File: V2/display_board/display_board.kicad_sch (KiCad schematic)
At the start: 52 parts, among them J1 Conn_01x12, J2 Conn_01x12, Q1 Si1308EDL, SW1 SW_Push, SW2 SW_Push, SW3 SW_Push, SW4 SW_Push, U1 TPS61165DBV, U2 LTR-303ALS-01, U3 DS18B20Z

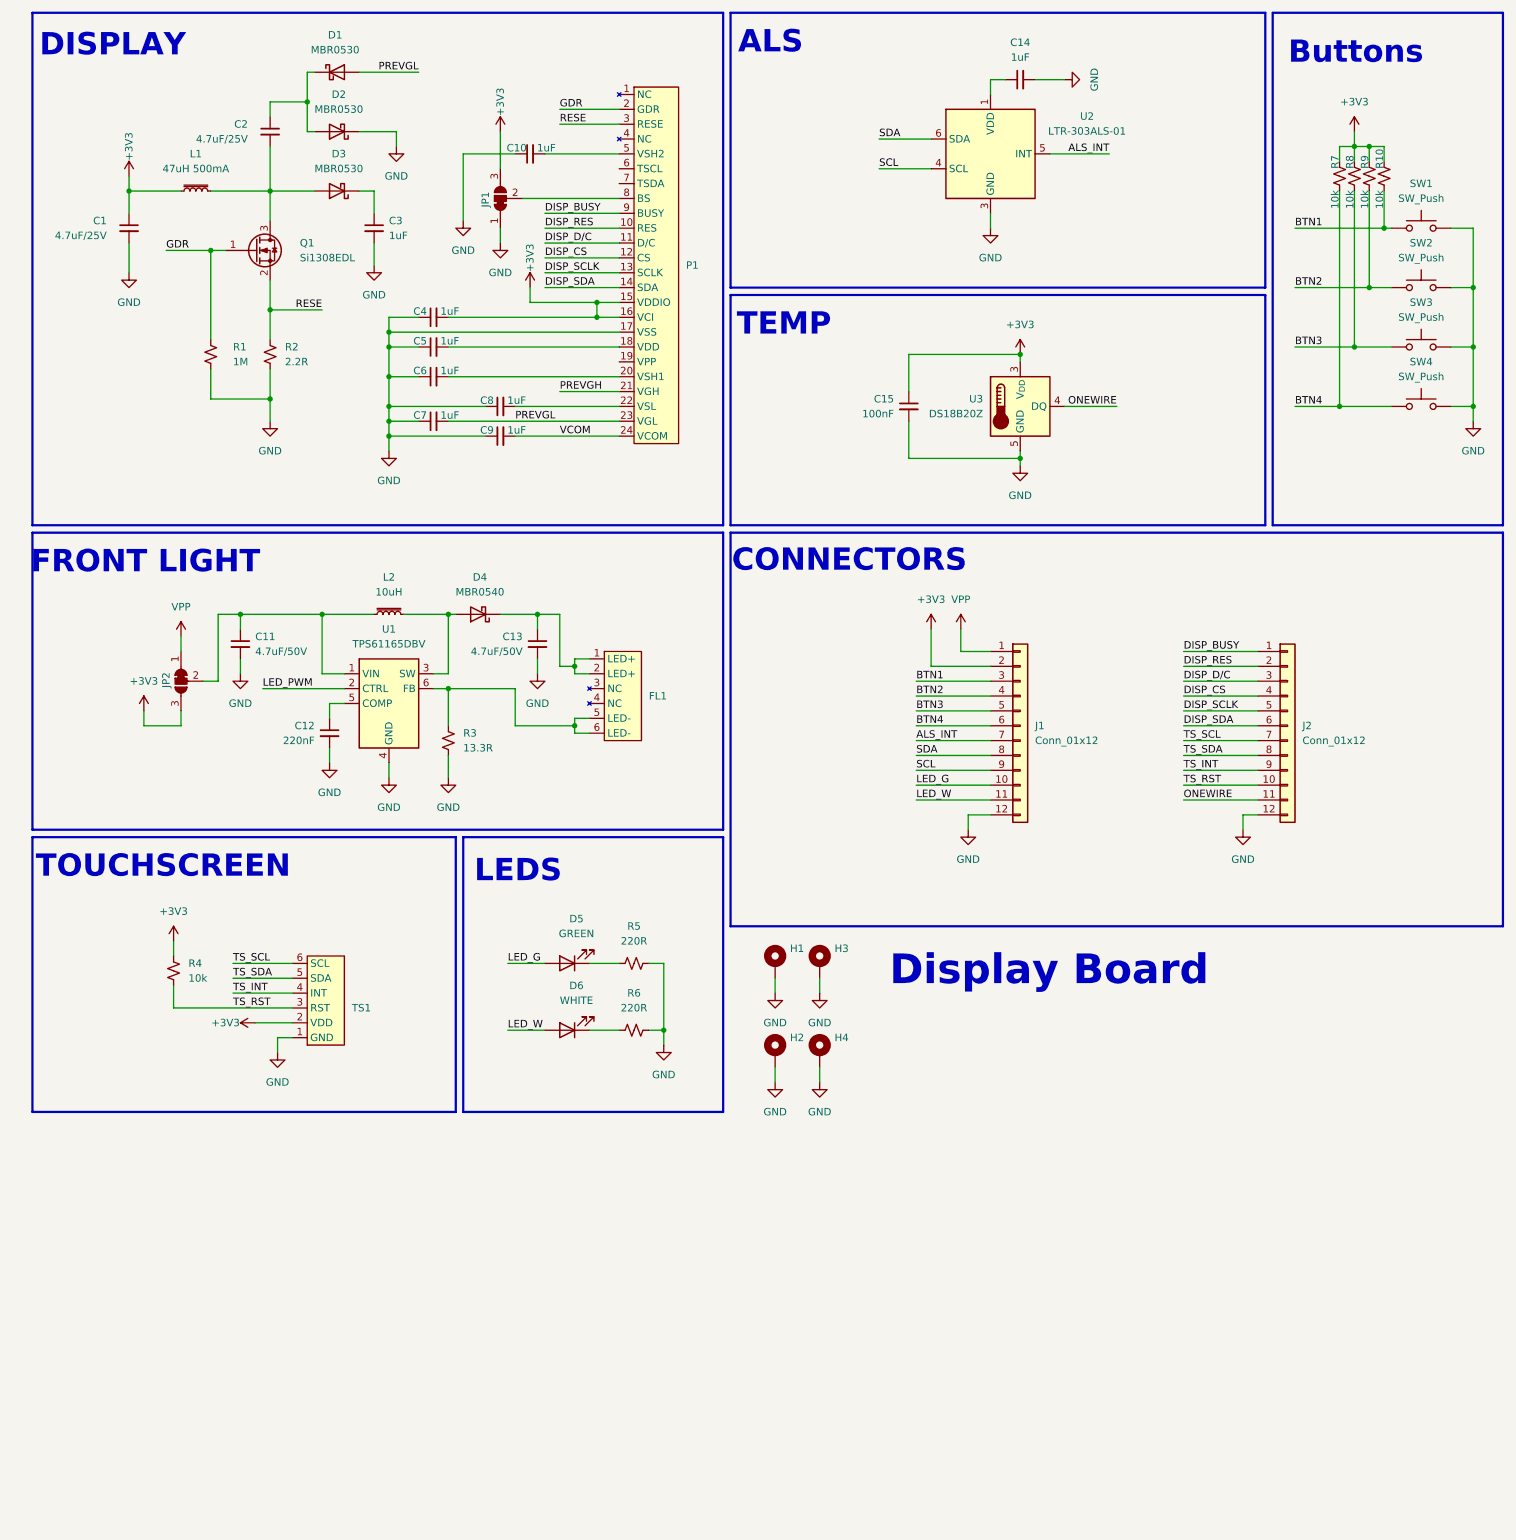
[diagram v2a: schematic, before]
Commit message: Initial component placement done.
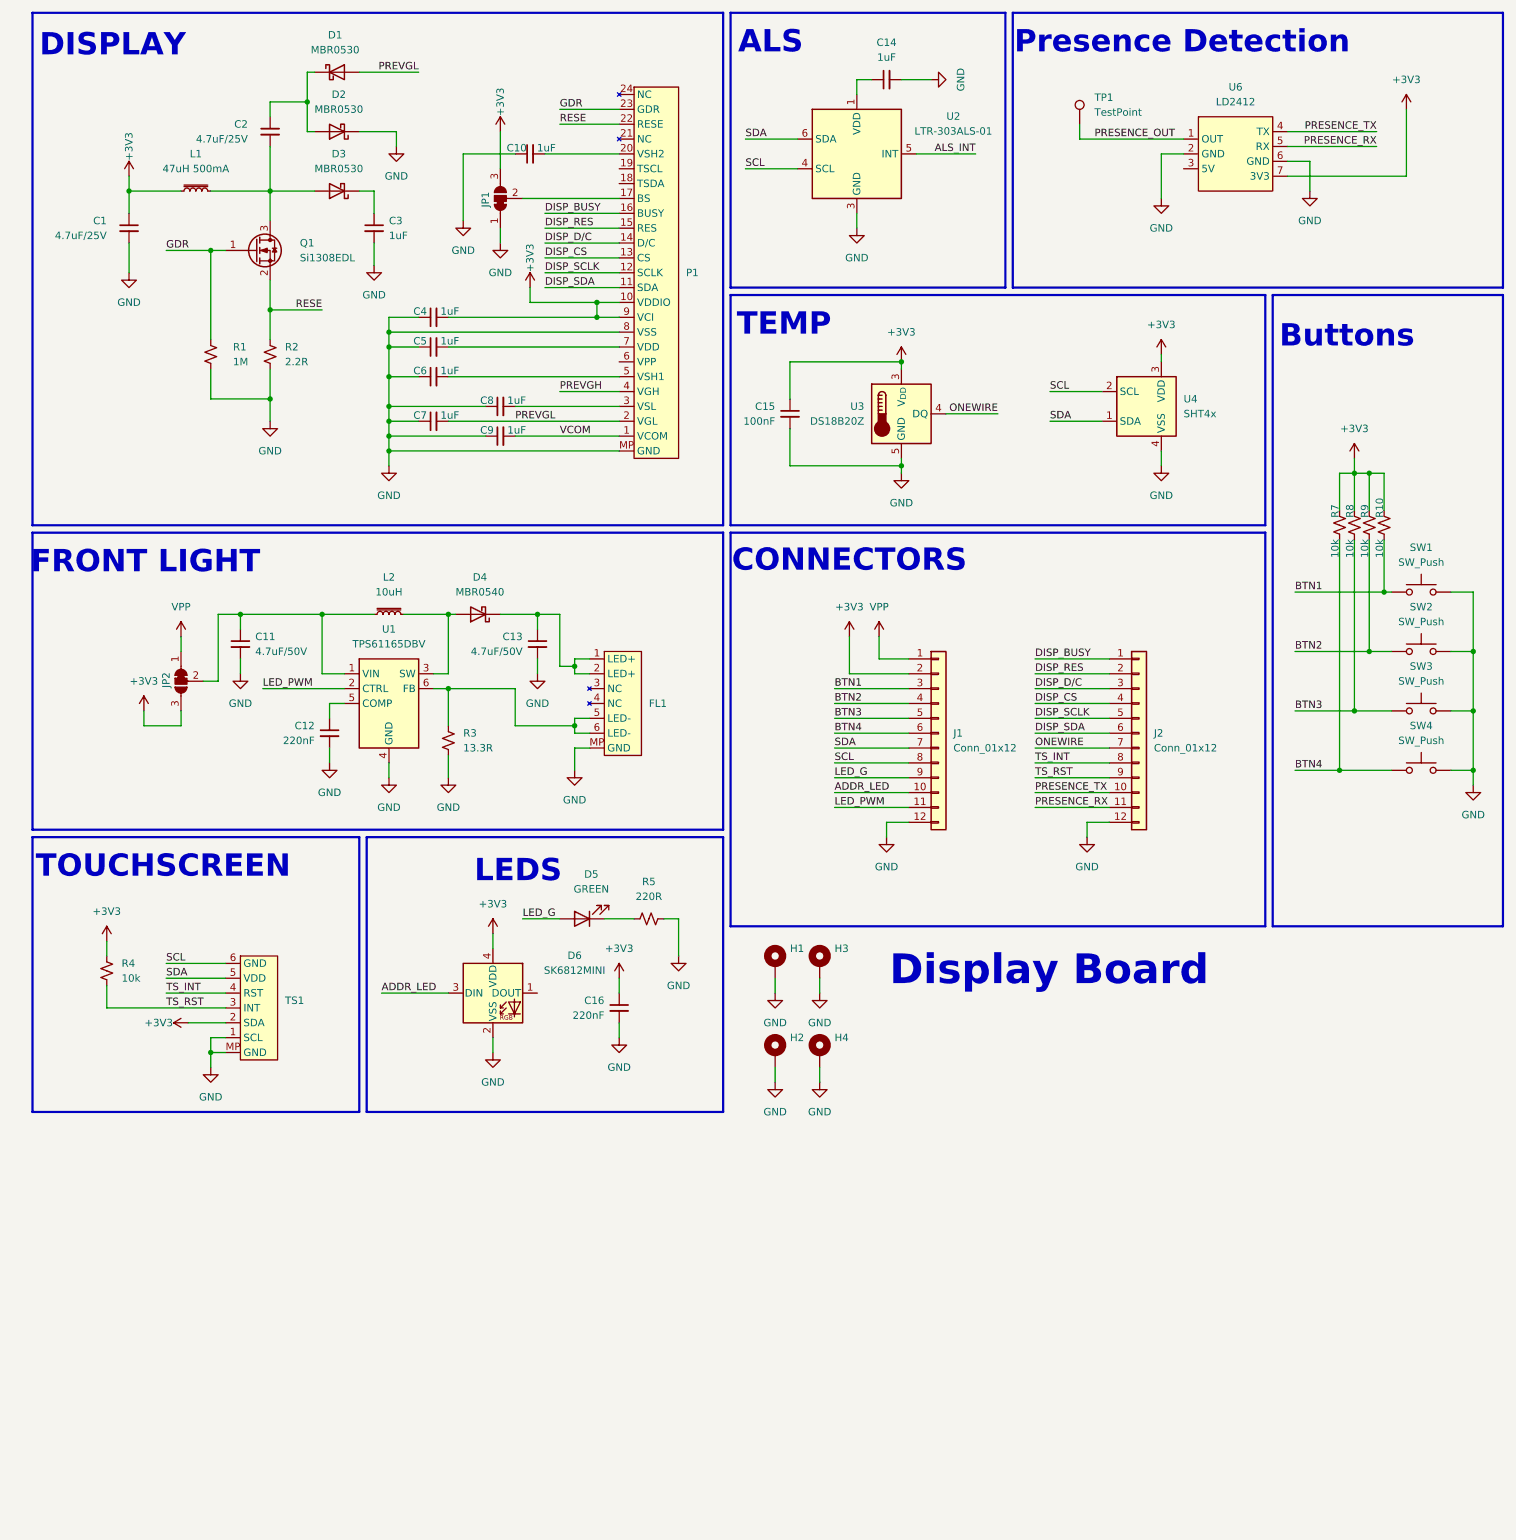
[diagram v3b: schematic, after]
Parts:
- removed D6: WHITE, LED_SMD:LED_0805_2012Metric, symbol *partsbox:KT-0805W
- removed R6: 220R, Resistor_SMD:R_0603_1608Metric, symbol *partsbox:0603-220ohm
- added C16: 220nF, Capacitor_SMD:C_0603_1608Metric, symbol *partsbox:0603-220nF
- added D6: SK6812MINI, LED_SMD:LED_SK6812MINI_PLCC4_3.5x3.5mm_P1.75mm, symbol *partsbox:SK6812MINI-HS
- added TP1: TestPoint, TestPoint:TestPoint_Pad_2.0x2.0mm, symbol Connector:TestPoint
- added U4: SHT4x, Sensor_Humidity:Sensirion_DFN-4_1.5x1.5mm_P0.8mm_SHT4x_NoCentralPad, symbol *partsbox:SHT41-AD1B-R2
- added U6: LD2412, MH_ics:LD2412, symbol *partsbox:LD2412
- L2: Manufacturer Taiyo Yuden -> TAIYO YUDEN
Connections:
- net LED_W is gone; now on net LED_PWM: J1.11 (Pin_11)
- net +3V3: now also P1.10 (VDDIO), P1.9 (VCI), C16.1, D6.4 (VDD), U4.3 (VDD), U6.7 (3V3); no longer P1.15 (VDDIO), P1.16 (VCI)
- net ALS_INT: no longer J1.7 (Pin_7)
- net DISP_BUSY: now also P1.16 (BUSY); no longer P1.9 (BUSY)
- net DISP_CS: now also P1.13 (CS); no longer P1.12 (CS)
- net DISP_D/C: now also P1.14 (D/C); no longer P1.11 (D/C)
- net DISP_RES: now also P1.15 (RES); no longer P1.10 (RES)
- net DISP_SCLK: now also P1.12 (SCLK); no longer P1.13 (SCLK)
- net DISP_SDA: now also P1.11 (SDA); no longer P1.14 (SDA)
- net GDR: now also P1.23 (GDR); no longer P1.2 (GDR)
- net GND: now also FL1.MP (GND), P1.8 (VSS), P1.MP (GND), TS1.MP (GND), C16.2, D6.2 (VSS), U4.4 (VSS), U6.2 (GND), U6.6 (GND); no longer P1.17 (VSS)
- net LED_G: now also J1.9 (Pin_9); no longer J1.10 (Pin_10)
- net ONEWIRE: now also J2.7 (Pin_7); no longer J2.11 (Pin_11)
- net PREVGH: now also P1.4 (VGH); no longer P1.21 (VGH)
- net PREVGL: now also P1.2 (VGL); no longer P1.23 (VGL)
- net RESE: now also P1.22 (RESE); no longer P1.3 (RESE)
- net SCL: now also J1.8 (Pin_8), TS1.6 (GND), U4.2 (SCL); no longer J1.9 (Pin_9)
- net SDA: now also J1.7 (Pin_7), TS1.5 (VDD), U4.1 (SDA); no longer J1.8 (Pin_8)
- net TS_INT: now also J2.8 (Pin_8); no longer J2.9 (Pin_9)
- net TS_RST: now also J2.9 (Pin_9); no longer J2.10 (Pin_10)
- net VCOM: now also P1.1 (VCOM); no longer P1.24 (VCOM)
- net at P1.18 (TSDA): no longer C5.2
- net at P1.20 (VSH2): now also C10.2; no longer C6.2
- net at C8.2: now also P1.3 (VSL); no longer P1.22 (VSL)
- net at P1.5 (VSH1): now also C6.2; no longer C10.2
- net at P1.7 (VDD): now also C5.2
- net at JP1.2 (C): now also P1.17 (BS); no longer P1.8 (BS)
- removed net TS_SCL: J2.7 (Pin_7), TS1.6 (SCL)
- removed net TS_SDA: J2.8 (Pin_8), TS1.5 (SDA)
- new net ADDR_LED: D6.3 (DIN), J1.10 (Pin_10)
- new net PRESENCE_OUT: TP1.1, U6.1 (OUT)
- new net PRESENCE_RX: J2.11 (Pin_11), U6.5 (RX)
- new net PRESENCE_TX: J2.10 (Pin_10), U6.4 (TX)
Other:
- note added: "Presence Detection"
- moved on the sheet: C14, C15, D5, J1, J2, R10, R4, R5, R7, R8, R9, SW1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

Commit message: In progress
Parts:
- added D7: GREEN, LED_SMD:LED_0805_2012Metric, symbol *partsbox:KT-0805G
- added D8: RED, LED_SMD:LED_0805_2012Metric, symbol *partsbox:NCD0805R1
- added J3: Conn_01x14, Connector_PinHeader_2.54mm:PinHeader_1x14_P2.54mm_Vertical_SMD_Pin1Left, symbol Connector_Generic:Conn_01x14
- added J4: Conn_01x14, Connector_PinSocket_2.54mm:PinSocket_1x14_P2.54mm_Vertical_SMD_Pin1Left, symbol Connector_Generic:Conn_01x14
- added R11, R6: 1.5K, Resistor_SMD:R_0603_1608Metric, symbol *partsbox:0603-1.5Kohm
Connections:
- net +3V3: now also J3.2 (Pin_2)
- net ADDR_LED: now also J3.10 (Pin_10)
- net BTN1: now also J3.3 (Pin_3)
- net BTN2: now also J3.4 (Pin_4)
- net BTN3: now also J3.5 (Pin_5)
- net BTN4: now also J3.6 (Pin_6)
- net DISP_BUSY: now also J4.1 (Pin_1)
- net DISP_CS: now also J4.4 (Pin_4)
- net DISP_D/C: now also J4.3 (Pin_3)
- net DISP_RES: now also J4.2 (Pin_2)
- net DISP_SCLK: now also J4.5 (Pin_5)
- net DISP_SDA: now also J4.6 (Pin_6)
- net GND: now also J3.11 (Pin_11), J3.14 (Pin_14), J4.12 (Pin_12), J4.14 (Pin_14)
- net LED_G: now also J3.9 (Pin_9)
- net LED_PWM: now also J4.13 (Pin_13)
- net ONEWIRE: now also J4.7 (Pin_7)
- net PRESENCE_RX: now also J4.11 (Pin_11)
- net PRESENCE_TX: now also J4.10 (Pin_10)
- net SCL: now also J3.8 (Pin_8)
- net SDA: now also J3.7 (Pin_7)
- net TS_INT: now also J4.8 (Pin_8)
- net TS_RST: now also J4.9 (Pin_9)
- net VPP: now also J3.1 (Pin_1), R11.2, R6.1
- new net: D7.1 (K), R6.2
- new net: D8.1 (K), R11.1
- new net CHG: J3.13 (Pin_13)
- new net PGOOD: J3.12 (Pin_12)

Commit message: Display board in good spot
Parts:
- removed J1, J2: Conn_01x12, Connector_PinHeader_2.54mm:PinHeader_1x12_P2.54mm_Vertical_SMD_Pin1Left, symbol *partsbox:TSM-112-01-SM-SV
- removed J3: Conn_01x14, Connector_PinHeader_2.54mm:PinHeader_1x14_P2.54mm_Vertical_SMD_Pin1Left, symbol Connector_Generic:Conn_01x14
- removed J4: Conn_01x14, Connector_PinSocket_2.54mm:PinSocket_1x14_P2.54mm_Vertical_SMD_Pin1Left, symbol Connector_Generic:Conn_01x14
- added J5: Conn_02x14_Top_Bottom, Connector_PinHeader_2.54mm:PinHeader_2x14_P2.54mm_Vertical_SMD, symbol Connector_Generic:Conn_02x14_Odd_Even
- H1, H2, H3, H4: footprint MountingHole:MountingHole_3.2mm_M3_ISO7380_Pad_TopBottom -> MountingHole:MountingHole_3.2mm_M3_ISO7380
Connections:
- net +3V3: now also C14.1, U2.1 (VDD), J5.3 (Pin_3)
- net ADDR_LED: now also J5.21 (Pin_21)
- net ALS_INT: now also J5.20 (Pin_20)
- net BTN1: now also J5.9 (Pin_9)
- net BTN2: now also J5.11 (Pin_11)
- net BTN3: now also J5.13 (Pin_13)
- net BTN4: now also J5.15 (Pin_15)
- net CHG: now also D8.2 (A), J5.26 (Pin_26)
- net DISP_BUSY: now also J5.2 (Pin_2)
- net DISP_CS: now also J5.8 (Pin_8)
- net DISP_D/C: now also J5.6 (Pin_6)
- net DISP_RES: now also J5.4 (Pin_4)
- net DISP_SCLK: now also J5.10 (Pin_10)
- net DISP_SDA: now also J5.12 (Pin_12)
- net GND: now also J5.23 (Pin_23), J5.27 (Pin_27), J5.28 (Pin_28)
- net LED_G: now also J5.22 (Pin_22)
- net LED_PWM: now also J5.25 (Pin_25)
- net ONEWIRE: now also J5.14 (Pin_14)
- net PGOOD: now also D7.2 (A), J5.24 (Pin_24)
- net PRESENCE_RX: now also J5.17 (Pin_17)
- net PRESENCE_TX: now also J5.19 (Pin_19)
- net PREVGH: now also C3.1, D3.1 (K)
- net TS_INT: now also J5.16 (Pin_16)
- net TS_RST: now also J5.18 (Pin_18)
- net VPP: now also J5.1 (Pin_1)
- net SCL renamed I2C_SCL
- net I2C_SCL: now also J5.7 (Pin_7)
- net SDA renamed I2C_SDA
- net I2C_SDA: now also J5.5 (Pin_5)
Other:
- moved on the sheet: C3, D7, D8, H1, H2, H3, H4, R11, R6

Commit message: fix symbol
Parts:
- added D10, D11, D12, D13, D14, D9: D_TVS, Diode_SMD:D_SOD-323, symbol *partsbox:H8VHD3B
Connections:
- net ADDR_LED: now also D13.2 (A2)
- net BTN1: now also D12.2 (A2)
- net BTN2: now also D11.2 (A2)
- net BTN3: now also D10.2 (A2)
- net BTN4: now also D9.2 (A2)
- net GND: now also D10.1 (A1), D11.1 (A1), D12.1 (A1), D13.1 (A1), D14.1 (A1), D9.1 (A1)
- net LED_G: now also D14.2 (A2)
- no-connect marks 0 -> 1
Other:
- moved on the sheet: D5, R10, R4, R5, R7, R8, R9, SW1, SW2, SW3, SW4, TS1

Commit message: Flip touch screen connector
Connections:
- net +3V3: now also TS1.5 (VDD); no longer TS1.2 (VDD)
- net GND: now also TS1.6 (GND); no longer TS1.1 (GND)
- net I2C_SCL: now also TS1.1 (SCL); no longer TS1.6 (SCL)
- net I2C_SDA: now also TS1.2 (SDA); no longer TS1.5 (SDA)
- net TS_INT: now also TS1.3 (INT); no longer TS1.4 (INT)
- net TS_RST: now also TS1.4 (RST); no longer TS1.3 (RST)
- net LED+: now reaches C13.1, D4.1 (K), FL1.1 (LED+), FL1.2 (LED+)
- net LED-: now reaches FL1.5 (LED-), FL1.6 (LED-), R3.1, U1.6 (FB)
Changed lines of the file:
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@@
+		)
+	)
+	(label "LED+"
+		(at 104.14 116.84 180)
+		(effects
+			(font
+				(size 1.27 1.27)
+			)
+			(justify right bottom)
 		)
 	)
@@
 		)
 	)
+	(label "LED-"
+		(at 104.14 135.89 180)
+		(effects
+			(font
+				(size 1.27 1.27)
+			)
+			(justify right bottom)
+		)
+	)
 	(label "DISP_BUSY"
 		(at 219.71 123.19 180)
@@
 		(pin "5"
 		)
+		(pin "1"
+		)
+		(pin "2"
+		)
+		(pin "4"
+		)
 		(pin "6"
 		)
-		(pin "2"
-		)
-		(pin "4"
-		)
-		(pin "1"
-		)
 		(pin "3"

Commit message: Finalize schematics
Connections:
- net GND: no longer J5.23 (Pin_23)
- net PRESENCE_OUT: now also J5.23 (Pin_23)
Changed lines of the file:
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@@
 	)
 	(junction
-		(at 120.65 165.1)
-		(diameter 0)
-		(color 0 0 0 0)
-	)
-	(junction
 		(at 240.03 123.19)
 		(diameter 0)
@@
 	)
 	(junction
-		(at 191.77 156.21)
-		(diameter 0)
-		(color 0 0 0 0)
-	)
-	(junction
 		(at 78.74 181.61)
 		(diameter 0)
@@
 	(wire
 		(pts
-			(xy 181.61 146.05) (xy 194.31 146.05)
+			(xy 180.34 146.05) (xy 194.31 146.05)
 		)
 		(stroke
@@
 	(wire
 		(pts
-			(xy 181.61 138.43) (xy 194.31 138.43)
+			(xy 180.34 138.43) (xy 194.31 138.43)
 		)
 		(stroke
@@
 	(wire
 		(pts
-			(xy 194.31 148.59) (xy 181.61 148.59)
+			(xy 194.31 148.59) (xy 180.34 148.59)
 		)
 		(stroke
@@
 	(wire
 		(pts
+			(xy 180.34 151.13) (xy 194.31 151.13)
+		)
+		(stroke
+			(width 0)
+			(type default)
+		)
+	)
+	(wire
+		(pts
 			(xy 229.87 133.35) (xy 237.49 133.35)
 		)
@@
 	(wire
 		(pts
-			(xy 181.61 128.27) (xy 194.31 128.27)
+			(xy 180.34 128.27) (xy 194.31 128.27)
 		)
 		(stroke
@@
 	(wire
 		(pts
-			(xy 194.31 151.13) (xy 191.77 151.13)
-		)
-		(stroke
-			(width 0)
-			(type default)
-		)
-	)
-	(wire
-		(pts
 			(xy 163.83 148.59) (xy 163.83 146.05)
 		)
@@
 	(wire
 		(pts
-			(xy 181.61 143.51) (xy 194.31 143.51)
+			(xy 180.34 143.51) (xy 194.31 143.51)
 		)
 		(stroke
@@
 	(wire
 		(pts
-			(xy 181.61 140.97) (xy 194.31 140.97)
+			(xy 180.34 140.97) (xy 194.31 140.97)
 		)
 		(stroke
@@
 		)
 	)
-	(wire
-		(pts
-			(xy 191.77 151.13) (xy 191.77 156.21)
-		)
-		(stroke
-			(width 0)
-			(type default)
-		)
-	)
 	(polyline
 		(pts
@@
 	(wire
 		(pts
-			(xy 181.61 133.35) (xy 194.31 133.35)
+			(xy 180.34 133.35) (xy 194.31 133.35)
 		)
 		(stroke
@@
 	(wire
 		(pts
-			(xy 181.61 130.81) (xy 194.31 130.81)
+			(xy 180.34 130.81) (xy 194.31 130.81)
 		)
 		(stroke
@@
 	(wire
 		(pts
-			(xy 119.38 165.1) (xy 120.65 165.1)
-		)
-		(stroke
-			(width 0)
-			(type default)
-		)
-	)
-	(wire
-		(pts
 			(xy 92.71 171.45) (xy 92.71 173.99)
 		)
@@
 	(wire
 		(pts
-			(xy 181.61 135.89) (xy 194.31 135.89)
+			(xy 180.34 135.89) (xy 194.31 135.89)
 		)
 		(stroke
@@
 	(wire
 		(pts
-			(xy 181.61 153.67) (xy 194.31 153.67)
+			(xy 180.34 153.67) (xy 194.31 153.67)
 		)
 		(stroke
@@
 	)
 	(label "BTN4"
-		(at 181.61 140.97 0)
+		(at 180.34 140.97 0)
 		(effects
 			(font
@@
 		)
 	)
+	(label "PRESENCE_OUT"
+		(at 180.34 151.13 0)
+		(effects
+			(font
+				(size 1.27 1.27)
+			)
+			(justify left bottom)
+		)
+	)
 	(label "BTN3"
-		(at 181.61 138.43 0)
+		(at 180.34 138.43 0)
 		(effects
 			(font
@@
 	)
 	(label "PRESENCE_TX"
-		(at 181.61 146.05 0)
+		(at 180.34 146.05 0)
 		(effects
 			(font
@@
 	)
 	(label "BTN2"
-		(at 181.61 135.89 0)
+		(at 180.34 135.89 0)
 		(effects
 			(font
@@
 	)
 	(label "I2C_SCL"
-		(at 181.61 130.81 0)
+		(at 180.34 130.81 0)
 		(effects
 			(font
@@
 	)
 	(label "ADDR_LED"
-		(at 181.61 148.59 0)
+		(at 180.34 148.59 0)
 		(effects
 			(font
@@
 	)
 	(label "PRESENCE_RX"
-		(at 181.61 143.51 0)
+		(at 180.34 143.51 0)
 		(effects
 			(font
@@
 	)
 	(label "BTN1"
-		(at 181.61 133.35 0)
+		(at 180.34 133.35 0)
 		(effects
 			(font
@@
 	)
 	(label "I2C_SDA"
-		(at 181.61 128.27 0)
+		(at 180.34 128.27 0)
 		(effects
 			(font
@@
 	)
 	(label "LED_G"
-		(at 119.38 165.1 0)
+		(at 120.65 165.1 0)
 		(effects
 			(font
@@
 	)
 	(label "LED_PWM"
-		(at 181.61 153.67 0)
+		(at 180.34 153.67 0)
 		(effects
 			(font
